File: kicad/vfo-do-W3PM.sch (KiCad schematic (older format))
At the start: 23 parts, among them J1 Fréquence, J10 GPS, J2 Bande, J3 Reset, J4 Résolution, J5 Si5351, J8 LCD, J9 Alim +12V, U1 L7805

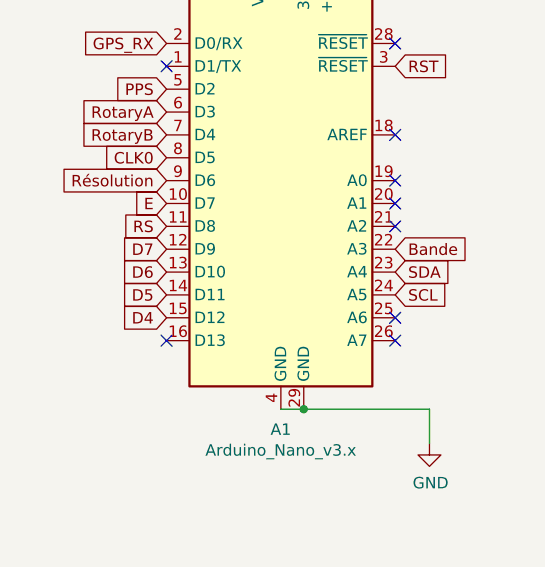
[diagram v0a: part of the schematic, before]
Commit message: Fix sens connecteur LCD
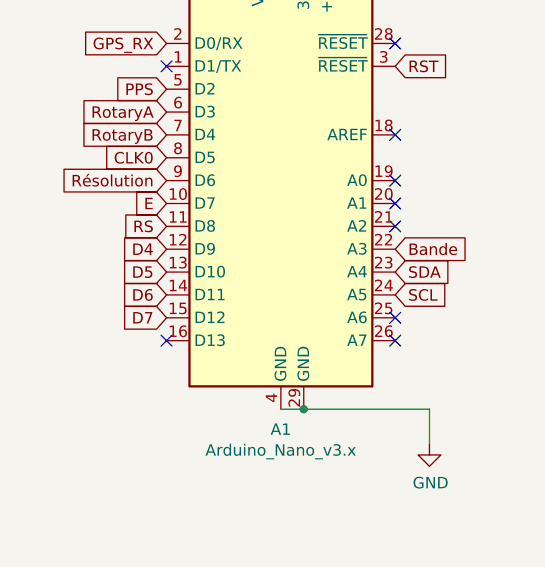
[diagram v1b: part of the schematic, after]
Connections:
- net D4: now also A1.12 (D9); no longer A1.15 (D12)
- net D5: now also A1.13 (D10); no longer A1.14 (D11)
- net D6: now also A1.14 (D11); no longer A1.13 (D10)
- net D7: now also A1.15 (D12); no longer A1.12 (D9)
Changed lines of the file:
@@
 Text GLabel 1150 4050 0    50   Input ~ 0
 E
+Text GLabel 1150 4250 0    50   Input ~ 0
+D4
+Text GLabel 1150 4350 0    50   Input ~ 0
+D5
+Text GLabel 1150 4450 0    50   Input ~ 0
+D6
 Text GLabel 1150 4550 0    50   Input ~ 0
-D4
-Text GLabel 1150 4450 0    50   Input ~ 0
-D5
-Text GLabel 1150 4350 0    50   Input ~ 0
-D6
-Text GLabel 1150 4250 0    50   Input ~ 0
 D7
 $Comp
